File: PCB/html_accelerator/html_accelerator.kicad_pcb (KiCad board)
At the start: 4 copper layers, 456.8 x 111.2 mm, 45 parts, among them J1 PCIexpress_bracket, J2 Bus_PCI_Express_x8, J3 PCIexpress_bracket, U10 48-TSOPI_12X20_MAC, U7 48-TSOPI_12X20_MAC, U8 48-TSOPI_12X20_MAC, U9 48-TSOPI_12X20_MAC

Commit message: Sch Symbol updates and cleanup
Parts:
- U10, U8, U9: value 48-TSOPI_12X20_MAC -> MX30LF1G28AD-TI
- U2, U4, U5: value ~ -> AU6438BS
- U3: value ~ -> MX30LF1G28AD-TI; footprint Package_SO:SSOP-28_3.9x9.9mm_P0.635mm -> html_accel_footprints:MX30LF1G28AD-TI
- U7: value 48-TSOPI_12X20_MAC -> AU6438BS; footprint html_accel_footprints:MX30LF1G28AD-TI -> Package_SO:SSOP-28_3.9x9.9mm_P0.635mm
- moved U3 30.4 mm to (49.1, 42.2)
- moved U7 28.4 mm to (71.8, 59.3)
- moved U4 5.91 mm to (71.8, 76.6)
- moved U5 4.67 mm to (71.8, 98.1)
- moved U8 1.85 mm to (49.1, 60.8)
- moved U2 1.59 mm to (71.8, 41.9)
- moved U9 1.54 mm to (49.1, 79.3)
- moved U10 1.27 mm to (49.1, 97.9)
- moved U6 0.25 mm to (92.2, 95.8)
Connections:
- J3 pad 1: (no net) -> unconnected-(J3-PTH1-Pad1)
- J3 pad 2: (no net) -> unconnected-(J3-PTH2-Pad2)
- U10 pad 16: unconnected-(U10B-CLE-Pad16) -> Net-(U10B-CLE)
- U10 pad 17: unconnected-(U10B-ALE-Pad17) -> Net-(U10B-ALE)
- U10 pad 18: unconnected-(U10B-WE#-Pad18) -> Net-(U10B-WE#)
- U10 pad 19: unconnected-(U10B-WP#-Pad19) -> Net-(U10B-WP#)
- U10 pad 38: unconnected-(U10B-PT-Pad38) -> Net-(U10B-PT)
- U10 pad 8: unconnected-(U10B-RE#-Pad8) -> Net-(U10B-RE#)
- U2 pad 1: (no net) -> unconnected-(U2-SDCDN-Pad1)
- U2 pad 10: (no net) -> unconnected-(U2-XTAL_IN-Pad10)
- U2 pad 11: (no net) -> unconnected-(U2-XTAL_OUT-Pad11)
- U2 pad 12: (no net) -> unconnected-(U2-VSS-Pad12)
- U2 pad 13: (no net) -> unconnected-(U2-VDD_1.8_OUT-Pad13)
- U2 pad 14: (no net) -> unconnected-(U2-VDD_FLASH_3.3_OUT-Pad14)
- U2 pad 15: (no net) -> unconnected-(U2-AVDD_5.0_OUT-Pad15)
- U2 pad 16: (no net) -> unconnected-(U2-VDD__3.3_OUT-Pad16)
- U2 pad 17: (no net) -> unconnected-(U2-VSSHM-Pad17)
- U2 pad 18: (no net) -> unconnected-(U2-MSINS-Pad18)
- U2 pad 19: (no net) -> unconnected-(U2-DATA2-Pad19)
- U2 pad 2: (no net) -> unconnected-(U2-SDWP-Pad2)
- U2 pad 20: (no net) -> unconnected-(U2-DATA3-Pad20)
- U2 pad 21: (no net) -> unconnected-(U2-DATA4-Pad21)
- U2 pad 22: (no net) -> unconnected-(U2-SDCMD-Pad22)
- U2 pad 23: (no net) -> unconnected-(U2-DATA5-Pad23)
- U2 pad 24: (no net) -> unconnected-(U2-SD_CLK-Pad24)
- U2 pad 25: (no net) -> unconnected-(U2-DATA6-Pad25)
- U2 pad 26: (no net) -> unconnected-(U2-DATA7-Pad26)
- U2 pad 27: (no net) -> unconnected-(U2-DATA0-Pad27)
- U2 pad 28: (no net) -> unconnected-(U2-DATA1-Pad28)
- U2 pad 3: (no net) -> unconnected-(U2-LED_ACTIVITY-Pad3)
- U2 pad 4: (no net) -> unconnected-(U2-CHIP_RST_N-Pad4)
- U2 pad 5: (no net) -> unconnected-(U2-EXT_R-Pad5)
- U2 pad 6: (no net) -> unconnected-(U2-V3.3_PHY_IN-Pad6)
- U2 pad 7: (no net) -> unconnected-(U2-USB_DP-Pad7)
- U2 pad 8: (no net) -> unconnected-(U2-USB_DN-Pad8)
- U2 pad 9: (no net) -> unconnected-(U2-VSSAREG-Pad9)
- U3 pad 1: (no net) -> unconnected-(U3A-NC-Pad1)
- U3 pad 10: (no net) -> unconnected-(U3A-NC-Pad10)
- U3 pad 11: (no net) -> unconnected-(U3A-NC-Pad11)
- U3 pad 12: (no net) -> unconnected-(U3A-VCC-Pad12)
- U3 pad 13: (no net) -> unconnected-(U3A-VSS-Pad13)
- U3 pad 14: (no net) -> unconnected-(U3A-NC-Pad14)
- U3 pad 15: (no net) -> unconnected-(U3A-NC-Pad15)
- U3 pad 16: (no net) -> unconnected-(U3B-CLE-Pad16)
- U3 pad 17: (no net) -> unconnected-(U3B-ALE-Pad17)
- U3 pad 18: (no net) -> unconnected-(U3B-WE#-Pad18)
- U3 pad 19: (no net) -> unconnected-(U3B-WP#-Pad19)
- U3 pad 2: (no net) -> unconnected-(U3A-NC-Pad2)
- U3 pad 20: (no net) -> unconnected-(U3A-NC-Pad20)
- U3 pad 21: (no net) -> unconnected-(U3A-NC-Pad21)
- U3 pad 22: (no net) -> unconnected-(U3A-NC-Pad22)
- U3 pad 23: (no net) -> unconnected-(U3A-NC-Pad23)
- U3 pad 24: (no net) -> unconnected-(U3A-NC-Pad24)
- U3 pad 25: (no net) -> unconnected-(U3A-VSS-Pad25)
- U3 pad 26: (no net) -> unconnected-(U3A-NC-Pad26)
- U3 pad 27: (no net) -> unconnected-(U3A-NC-Pad27)
- U3 pad 28: (no net) -> unconnected-(U3A-NC-Pad28)
- U3 pad 3: (no net) -> unconnected-(U3A-NC-Pad3)
- U3 pad 4: (no net) -> unconnected-(U3A-NC-Pad4)
- U3 pad 5: (no net) -> unconnected-(U3A-NC-Pad5)
- U3 pad 6: (no net) -> unconnected-(U3A-NC-Pad6)
- U3 pad 7: (no net) -> Net-(U3B-R/B#)
- U3 pad 8: (no net) -> unconnected-(U3B-RE#-Pad8)
- U3 pad 9: (no net) -> unconnected-(U3B-CE#-Pad9)
- U4 pad 1: (no net) -> unconnected-(U4-SDCDN-Pad1)
- U4 pad 10: (no net) -> unconnected-(U4-XTAL_IN-Pad10)
- U4 pad 11: (no net) -> unconnected-(U4-XTAL_OUT-Pad11)
- U4 pad 12: (no net) -> unconnected-(U4-VSS-Pad12)
- U4 pad 13: (no net) -> unconnected-(U4-VDD_1.8_OUT-Pad13)
- U4 pad 14: (no net) -> unconnected-(U4-VDD_FLASH_3.3_OUT-Pad14)
- U4 pad 15: (no net) -> unconnected-(U4-AVDD_5.0_OUT-Pad15)
- U4 pad 16: (no net) -> unconnected-(U4-VDD__3.3_OUT-Pad16)
- U4 pad 17: (no net) -> unconnected-(U4-VSSHM-Pad17)
- U4 pad 18: (no net) -> unconnected-(U4-MSINS-Pad18)
- U4 pad 19: (no net) -> unconnected-(U4-DATA2-Pad19)
- U4 pad 2: (no net) -> unconnected-(U4-SDWP-Pad2)
- U4 pad 20: (no net) -> unconnected-(U4-DATA3-Pad20)
- U4 pad 21: (no net) -> unconnected-(U4-DATA4-Pad21)
- U4 pad 22: (no net) -> unconnected-(U4-SDCMD-Pad22)
- U4 pad 23: (no net) -> unconnected-(U4-DATA5-Pad23)
- U4 pad 24: (no net) -> unconnected-(U4-SD_CLK-Pad24)
- U4 pad 25: (no net) -> unconnected-(U4-DATA6-Pad25)
- U4 pad 26: (no net) -> unconnected-(U4-DATA7-Pad26)
- U4 pad 27: (no net) -> unconnected-(U4-DATA0-Pad27)
- U4 pad 28: (no net) -> unconnected-(U4-DATA1-Pad28)
- U4 pad 3: (no net) -> unconnected-(U4-LED_ACTIVITY-Pad3)
- U4 pad 4: (no net) -> unconnected-(U4-CHIP_RST_N-Pad4)
- U4 pad 5: (no net) -> unconnected-(U4-EXT_R-Pad5)
- U4 pad 6: (no net) -> unconnected-(U4-V3.3_PHY_IN-Pad6)
- U4 pad 7: (no net) -> unconnected-(U4-USB_DP-Pad7)
- U4 pad 8: (no net) -> unconnected-(U4-USB_DN-Pad8)
- U4 pad 9: (no net) -> unconnected-(U4-VSSAREG-Pad9)
- U5 pad 1: (no net) -> unconnected-(U5-SDCDN-Pad1)
- U5 pad 10: (no net) -> unconnected-(U5-XTAL_IN-Pad10)
- U5 pad 11: (no net) -> unconnected-(U5-XTAL_OUT-Pad11)
- U5 pad 12: (no net) -> unconnected-(U5-VSS-Pad12)
- U5 pad 13: (no net) -> unconnected-(U5-VDD_1.8_OUT-Pad13)
- U5 pad 14: (no net) -> unconnected-(U5-VDD_FLASH_3.3_OUT-Pad14)
- U5 pad 15: (no net) -> unconnected-(U5-AVDD_5.0_OUT-Pad15)
- U5 pad 16: (no net) -> unconnected-(U5-VDD__3.3_OUT-Pad16)
- U5 pad 17: (no net) -> unconnected-(U5-VSSHM-Pad17)
- U5 pad 18: (no net) -> unconnected-(U5-MSINS-Pad18)
- U5 pad 19: (no net) -> unconnected-(U5-DATA2-Pad19)
- U5 pad 2: (no net) -> unconnected-(U5-SDWP-Pad2)
- U5 pad 20: (no net) -> unconnected-(U5-DATA3-Pad20)
- U5 pad 21: (no net) -> unconnected-(U5-DATA4-Pad21)
- U5 pad 22: (no net) -> unconnected-(U5-SDCMD-Pad22)
- U5 pad 23: (no net) -> unconnected-(U5-DATA5-Pad23)
- U5 pad 24: (no net) -> unconnected-(U5-SD_CLK-Pad24)
- U5 pad 25: (no net) -> unconnected-(U5-DATA6-Pad25)
- U5 pad 26: (no net) -> unconnected-(U5-DATA7-Pad26)
- U5 pad 27: (no net) -> unconnected-(U5-DATA0-Pad27)
- U5 pad 28: (no net) -> unconnected-(U5-DATA1-Pad28)
- U5 pad 3: (no net) -> unconnected-(U5-LED_ACTIVITY-Pad3)
- U5 pad 4: (no net) -> unconnected-(U5-CHIP_RST_N-Pad4)
- U5 pad 5: (no net) -> unconnected-(U5-EXT_R-Pad5)
- U5 pad 6: (no net) -> unconnected-(U5-V3.3_PHY_IN-Pad6)
- U5 pad 7: (no net) -> unconnected-(U5-USB_DP-Pad7)
- U5 pad 8: (no net) -> unconnected-(U5-USB_DN-Pad8)
- U5 pad 9: (no net) -> unconnected-(U5-VSSAREG-Pad9)
- U8 pad 16: unconnected-(U8B-CLE-Pad16) -> Net-(U3B-I/O0)
- U8 pad 17: unconnected-(U8B-ALE-Pad17) -> Net-(U3B-R/B#)
- U8 pad 18: unconnected-(U8B-WE#-Pad18) -> Net-(U3B-I/O5)
- U8 pad 19: unconnected-(U8B-WP#-Pad19) -> Net-(U3B-I/O6)
- U8 pad 38: unconnected-(U8B-PT-Pad38) -> Net-(U3B-I/O1)
- U8 pad 8: unconnected-(U8B-RE#-Pad8) -> Net-(U3B-I/O3)
- U9 pad 29: unconnected-(U9B-I/O0-Pad29) -> Net-(U10B-CLE)
- U9 pad 30: unconnected-(U9B-I/O1-Pad30) -> Net-(U10B-PT)
- U9 pad 32: unconnected-(U9B-I/O3-Pad32) -> Net-(U10B-RE#)
- U9 pad 42: unconnected-(U9B-I/O5-Pad42) -> Net-(U10B-WE#)
- U9 pad 43: unconnected-(U9B-I/O6-Pad43) -> Net-(U10B-WP#)
- U9 pad 7: unconnected-(U9B-R/B#-Pad7) -> Net-(U10B-ALE)
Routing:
- net +12V: track 2.62 -> 0.00 mm, vias 2 -> 0
- net (no net): track 0.00 -> 2.62 mm, vias 0 -> 2

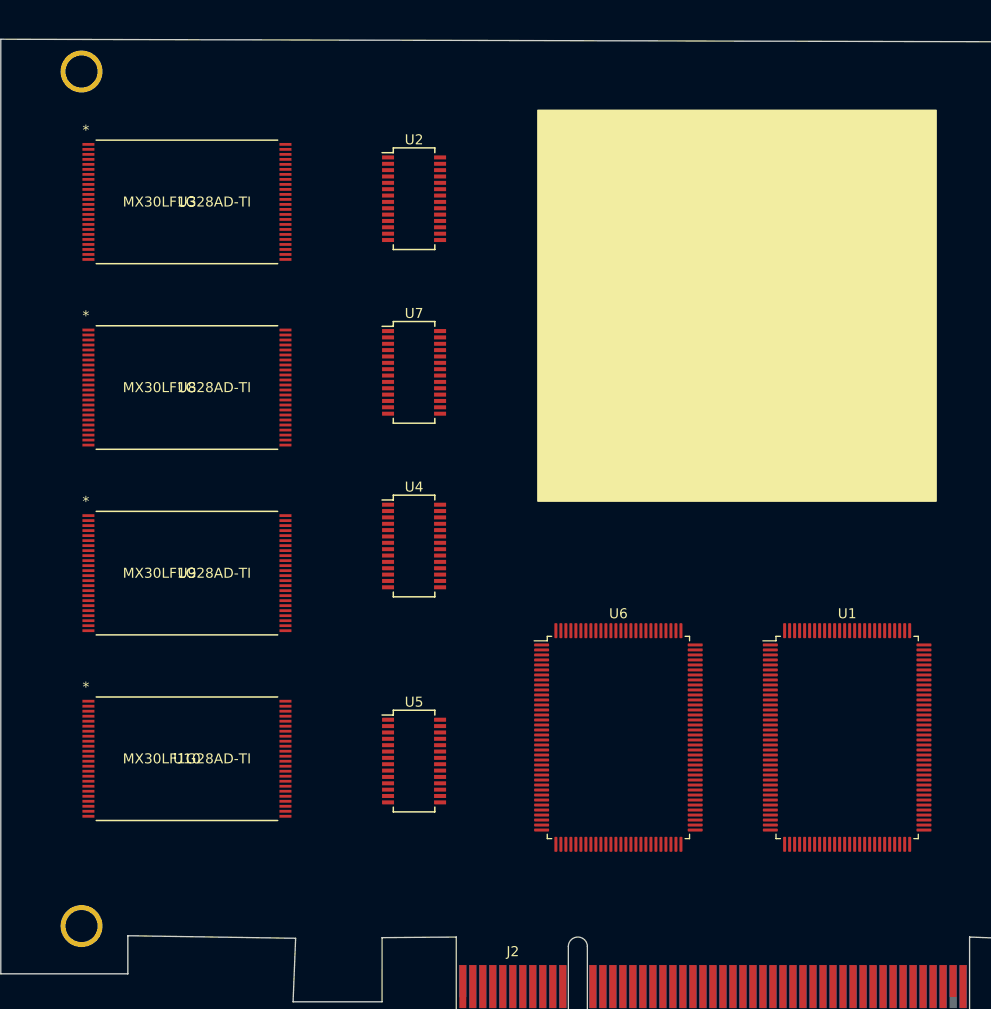
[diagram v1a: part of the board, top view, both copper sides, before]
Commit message: Update to MCS9990 for PCIE direct to USB
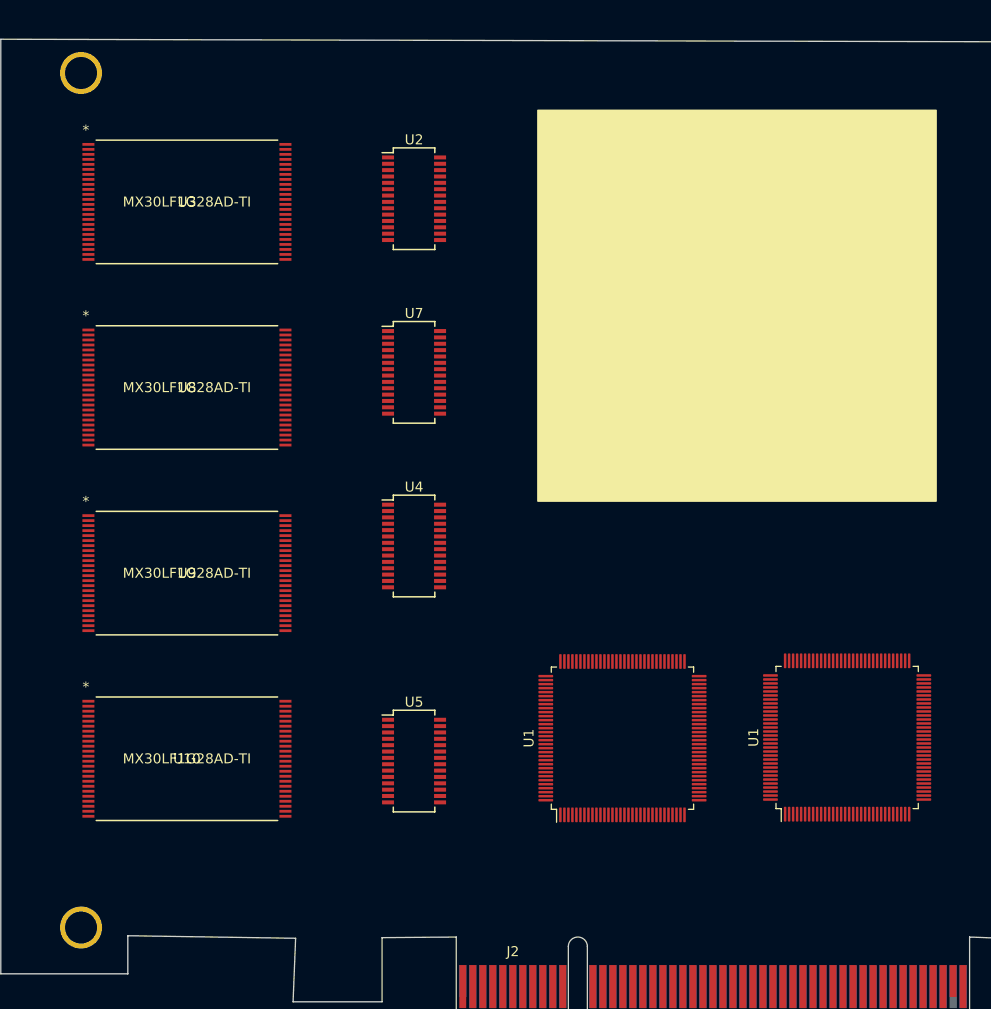
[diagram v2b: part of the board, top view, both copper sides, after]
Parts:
- removed J3: PCIexpress_bracket, html_accel_footprints:PCIexpress_bracket_full
- removed U6: ~, Package_QFP:LQFP-128_14x20mm_P0.5mm
- added U1: MCS9990, Package_QFP:LQFP-128_14x14mm_P0.4mm, F.Cu at (92.6, 95.8)
- J1: footprint PCIexpress:PCIexpress_bracket_full -> html_accel_footprints:PCIexpress_bracket_full
- U1: value ~ -> MCS9990; footprint Package_QFP:LQFP-128_14x20mm_P0.5mm -> Package_QFP:LQFP-128_14x14mm_P0.4mm
- moved J1 357.1 mm to (76.2, 124.1)
- turned U1 to 90 degrees
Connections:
- U1 pad 1: (no net) -> unconnected-(U1A-GND1-Pad1)
- U1 pad 10: (no net) -> unconnected-(U1C-PCIE_RXDP-Pad10)
- U1 pad 100: (no net) -> unconnected-(U1D-USB0_PWR_EN_N-Pad100)
- U1 pad 101: (no net) -> unconnected-(U1E-LN_STAT2-Pad101)
- U1 pad 102: (no net) -> unconnected-(U1D-USB1_OVCI_N-Pad102)
- U1 pad 103: (no net) -> unconnected-(U1D-USB1_PWR_EN_N-Pad103)
- U1 pad 104: (no net) -> unconnected-(U1E-LN_STAT0-Pad104)
- U1 pad 105: (no net) -> unconnected-(U1E-LN_STAT1-Pad105)
- U1 pad 106: (no net) -> unconnected-(U1A-+3.3VIO-Pad106)
- U1 pad 107: (no net) -> unconnected-(U1A-GND20-Pad107)
- U1 pad 108: (no net) -> unconnected-(U1A-GND21-Pad108)
- U1 pad 109: (no net) -> unconnected-(U1A-+1.2V-Pad109)
- U1 pad 11: (no net) -> unconnected-(U1A-GND3-Pad11)
- U1 pad 110: (no net) -> unconnected-(U1A-+3.3VA-Pad110)
- U1 pad 111: (no net) -> unconnected-(U1A-+3.3VA-Pad111)
- U1 pad 112: (no net) -> unconnected-(U1D-USB2_DM-Pad112)
- U1 pad 113: (no net) -> unconnected-(U1D-USB2_DP-Pad113)
- U1 pad 114: (no net) -> unconnected-(U1A-GND22-Pad114)
- U1 pad 115: (no net) -> unconnected-(U1A-GND23-Pad115)
- U1 pad 116: (no net) -> unconnected-(U1D-USB2_IBERF-Pad116)
- U1 pad 117: (no net) -> unconnected-(U1D-USB2_OTG_VBUS-Pad117)
- U1 pad 118: (no net) -> unconnected-(U1A-GND24-Pad118)
- U1 pad 119: (no net) -> unconnected-(U1A-+3.3VA-Pad119)
- U1 pad 12: (no net) -> unconnected-(U1A-+1.2VA-Pad12)
- U1 pad 120: (no net) -> unconnected-(U1A-GND25-Pad120)
- U1 pad 121: (no net) -> unconnected-(U1A-+1.2V-Pad121)
- U1 pad 122: (no net) -> unconnected-(U1D-USB2_OVCI_N-Pad122)
- U1 pad 123: (no net) -> unconnected-(U1D-USB2_PWR_EN_N-Pad123)
- U1 pad 124: (no net) -> unconnected-(U1D-USB2_OTG_ID-Pad124)
- U1 pad 125: (no net) -> unconnected-(U1D-USB3_OVCI_N-Pad125)
- U1 pad 126: (no net) -> unconnected-(U1D-USB3_PWR_EN_N-Pad126)
- U1 pad 127: (no net) -> unconnected-(U1A-+3.3VIO-Pad127)
- U1 pad 128: (no net) -> unconnected-(U1A-GND26-Pad128)
- U1 pad 13: (no net) -> unconnected-(U1C-PCIE_TXDP-Pad13)
- U1 pad 14: (no net) -> unconnected-(U1C-PCIE_TXDN-Pad14)
- U1 pad 15: (no net) -> unconnected-(U1A-+1.2VA-Pad15)
- U1 pad 16: (no net) -> unconnected-(U1A-+3.3VA_PLL-Pad16)
- U1 pad 17: (no net) -> unconnected-(U1A-GND4-Pad17)
- U1 pad 18: (no net) -> unconnected-(U1A-GND5-Pad18)
- U1 pad 19: (no net) -> unconnected-(U1A-+3.3VA_AUX-Pad19)
- U1 pad 2: (no net) -> unconnected-(U1A-+3.3VIN_REG-Pad2)
- U1 pad 20: (no net) -> unconnected-(U1A-+1.2V-Pad20)
- U1 pad 21: (no net) -> unconnected-(U1A-GND6-Pad21)
- U1 pad 22: (no net) -> unconnected-(U1C-PCIE_CLKREQ_N-Pad22)
- U1 pad 23: (no net) -> unconnected-(U1C-PCIE_WAKE_N-Pad23)
- U1 pad 24: (no net) -> unconnected-(U1E-MODE_SEL0-Pad24)
- U1 pad 25: (no net) -> unconnected-(U1A-+3.3VIO-Pad25)
- U1 pad 26: (no net) -> unconnected-(U1A-GND7-Pad26)
- U1 pad 27: (no net) -> unconnected-(U1E-OTG_EN_N-Pad27)
- U1 pad 28: (no net) -> unconnected-(U1C-PCIE_PERST_N-Pad28)
- U1 pad 29: (no net) -> unconnected-(U1E-EE_SCL-Pad29)
- U1 pad 3: (no net) -> unconnected-(U1A-+1.2VOUT_REG-Pad3)
- U1 pad 30: (no net) -> unconnected-(U1E-EE_SDA-Pad30)
- U1 pad 31: (no net) -> unconnected-(U1E-SCAN_EN-Pad31)
- U1 pad 32: (no net) -> unconnected-(U1E-TEST_EN-Pad32)
- U1 pad 33: (no net) -> unconnected-(U1A-+1.2V-Pad33)
- U1 pad 34: (no net) -> unconnected-(U1A-GND8-Pad34)
- U1 pad 35: (no net) -> unconnected-(U1B-GPIO0/D0-Pad35)
- U1 pad 36: (no net) -> unconnected-(U1B-GPIO1/D1-Pad36)
- U1 pad 37: (no net) -> unconnected-(U1B-GPIO2/D2-Pad37)
- U1 pad 38: (no net) -> unconnected-(U1B-GPIO3/D3-Pad38)
- U1 pad 39: (no net) -> unconnected-(U1B-GPIO4/D4-Pad39)
- U1 pad 4: (no net) -> unconnected-(U1C-PCIE_REFCLKN-Pad4)
- U1 pad 40: (no net) -> unconnected-(U1B-GPIO5/D5-Pad40)
- U1 pad 41: (no net) -> unconnected-(U1B-GPIO6/D6-Pad41)
- U1 pad 42: (no net) -> unconnected-(U1B-GPIO7/D7-Pad42)
- U1 pad 43: (no net) -> unconnected-(U1B-GPIO8/INTA-Pad43)
- U1 pad 44: (no net) -> unconnected-(U1B-GPIO9/INTB-Pad44)
- U1 pad 45: (no net) -> unconnected-(U1B-GPIO10/INTC-Pad45)
- U1 pad 46: (no net) -> unconnected-(U1B-GPIO11/INTD-Pad46)
- U1 pad 47: (no net) -> unconnected-(U1E-MODE_SEL1-Pad47)
- U1 pad 48: (no net) -> unconnected-(U1A-+3.3VIO-Pad48)
- U1 pad 49: (no net) -> unconnected-(U1E-MODE_SEL2-Pad49)
- U1 pad 5: (no net) -> unconnected-(U1C-PCIE_REFCLKP-Pad5)
- U1 pad 50: (no net) -> unconnected-(U1A-GND9-Pad50)
- U1 pad 51: (no net) -> unconnected-(U1A-+3.3VA-Pad51)
- U1 pad 52: (no net) -> unconnected-(U1A-+3.3VA-Pad52)
- U1 pad 53: (no net) -> unconnected-(U1D-USB3_DM-Pad53)
- U1 pad 54: (no net) -> unconnected-(U1D-USB3_DP-Pad54)
- U1 pad 55: (no net) -> unconnected-(U1A-GND10-Pad55)
- U1 pad 56: (no net) -> unconnected-(U1A-GND11-Pad56)
- U1 pad 57: (no net) -> unconnected-(U1D-USB3_IBREF-Pad57)
- U1 pad 58: (no net) -> unconnected-(U1A-+1.2V-Pad58)
- U1 pad 59: (no net) -> unconnected-(U1A-GND12-Pad59)
- U1 pad 6: (no net) -> unconnected-(U1A-+1.2VA_AUX-Pad6)
- U1 pad 60: (no net) -> unconnected-(U1E-JTAG_TCK-Pad60)
- U1 pad 61: (no net) -> unconnected-(U1E-JTAG_TDI-Pad61)
- U1 pad 62: (no net) -> unconnected-(U1E-JTAG_TDO-Pad62)
- U1 pad 63: (no net) -> unconnected-(U1E-JTAG_TMS-Pad63)
- U1 pad 64: (no net) -> unconnected-(U1E-JTAG_TRST_N-Pad64)
- U1 pad 65: (no net) -> unconnected-(U1B-GPIO12/CSA_N-Pad65)
- U1 pad 66: (no net) -> unconnected-(U1B-GPIO13/CSB_N-Pad66)
- U1 pad 67: (no net) -> unconnected-(U1B-GPIO14/CSC_N-Pad67)
- U1 pad 68: (no net) -> unconnected-(U1B-GPIO15/CSD_N-Pad68)
- U1 pad 69: (no net) -> unconnected-(U1A-GND13-Pad69)
- U1 pad 7: (no net) -> unconnected-(U1C-REXT-Pad7)
- U1 pad 70: (no net) -> unconnected-(U1A-+3.3VIO-Pad70)
- U1 pad 71: (no net) -> unconnected-(U1B-GPIO16/RESET-Pad71)
- U1 pad 72: (no net) -> unconnected-(U1B-GPIO17/IOW_N-Pad72)
- U1 pad 73: (no net) -> unconnected-(U1B-GPIO18/IOR_N-Pad73)
- U1 pad 74: (no net) -> unconnected-(U1B-GPIO23/IOCHRDY2-Pad74)
- U1 pad 75: (no net) -> unconnected-(U1B-GPIO19/A0-Pad75)
- U1 pad 76: (no net) -> unconnected-(U1B-GPIO20/A1-Pad76)
- U1 pad 77: (no net) -> unconnected-(U1B-GPIO21/A2-Pad77)
- U1 pad 78: (no net) -> unconnected-(U1B-GPIO22/IOCHRDY1-Pad78)
- U1 pad 79: (no net) -> unconnected-(U1A-GND14-Pad79)
- U1 pad 8: (no net) -> unconnected-(U1A-GND2-Pad8)
- U1 pad 80: (no net) -> unconnected-(U1A-+1.2V-Pad80)
- U1 pad 81: (no net) -> unconnected-(U1D-USB0_XSCI-Pad81)
- U1 pad 82: (no net) -> unconnected-(U1D-USB0_XSCO-Pad82)
- U1 pad 83: (no net) -> unconnected-(U1A-+3.3VA-Pad83)
- U1 pad 84: (no net) -> unconnected-(U1A-+3.3VA-Pad84)
- U1 pad 85: (no net) -> unconnected-(U1D-USB0_DM-Pad85)
- U1 pad 86: (no net) -> unconnected-(U1D-USB0_DP-Pad86)
- U1 pad 87: (no net) -> unconnected-(U1A-GND15-Pad87)
- U1 pad 88: (no net) -> unconnected-(U1A-GND16-Pad88)
- U1 pad 89: (no net) -> unconnected-(U1D-USB0_IBREF-Pad89)
- U1 pad 9: (no net) -> unconnected-(U1C-PCIE_RXDN-Pad9)
- U1 pad 90: (no net) -> unconnected-(U1A-+3.3VA-Pad90)
- U1 pad 91: (no net) -> unconnected-(U1A-+3.3VA-Pad91)
- U1 pad 92: (no net) -> unconnected-(U1D-USB1_DM-Pad92)
- U1 pad 93: (no net) -> unconnected-(U1D-USB1_DP-Pad93)
- U1 pad 94: (no net) -> unconnected-(U1A-GND17-Pad94)
- U1 pad 95: (no net) -> unconnected-(U1A-GND18-Pad95)
- U1 pad 96: (no net) -> unconnected-(U1D-USB1_IBREF-Pad96)
- U1 pad 97: (no net) -> unconnected-(U1A-GND19-Pad97)
- U1 pad 98: (no net) -> unconnected-(U1A-+1.2V-Pad98)
- U1 pad 99: (no net) -> unconnected-(U1D-USB0_OVCI_N-Pad99)
- U10 pad 16: Net-(U10B-CLE) -> unconnected-(U10B-#CMD_LATCH_EN-Pad16)
- U10 pad 17: Net-(U10B-ALE) -> unconnected-(U10B-ADDR_LATCH-Pad17)
- U10 pad 18: Net-(U10B-WE#) -> unconnected-(U10B-#WRITE_EN-Pad18)
- U10 pad 19: Net-(U10B-WP#) -> unconnected-(U10B-#WRITE_PROT-Pad19)
- U10 pad 38: Net-(U10B-PT) -> unconnected-(U10B-PROTECT-Pad38)
- U10 pad 8: Net-(U10B-RE#) -> unconnected-(U10B-#READ_EN-Pad8)
- U3 pad 29: Net-(U3B-I/O0) -> unconnected-(U3B-I/O0-Pad29)
- U3 pad 30: Net-(U3B-I/O1) -> unconnected-(U3B-I/O1-Pad30)
- U3 pad 32: Net-(U3B-I/O3) -> unconnected-(U3B-I/O3-Pad32)
- U3 pad 42: Net-(U3B-I/O5) -> unconnected-(U3B-I/O5-Pad42)
- U3 pad 43: Net-(U3B-I/O6) -> unconnected-(U3B-I/O6-Pad43)
- U3 pad 7: Net-(U3B-R/B#) -> unconnected-(U3B-STATUS-Pad7)
- U8 pad 16: Net-(U3B-I/O0) -> unconnected-(U8B-#CMD_LATCH_EN-Pad16)
- U8 pad 17: Net-(U3B-R/B#) -> unconnected-(U8B-ADDR_LATCH-Pad17)
- U8 pad 18: Net-(U3B-I/O5) -> unconnected-(U8B-#WRITE_EN-Pad18)
- U8 pad 19: Net-(U3B-I/O6) -> unconnected-(U8B-#WRITE_PROT-Pad19)
- U8 pad 38: Net-(U3B-I/O1) -> unconnected-(U8B-PROTECT-Pad38)
- U8 pad 8: Net-(U3B-I/O3) -> unconnected-(U8B-#READ_EN-Pad8)
- U9 pad 29: Net-(U10B-CLE) -> unconnected-(U9B-I/O0-Pad29)
- U9 pad 30: Net-(U10B-PT) -> unconnected-(U9B-I/O1-Pad30)
- U9 pad 32: Net-(U10B-RE#) -> unconnected-(U9B-I/O3-Pad32)
- U9 pad 42: Net-(U10B-WE#) -> unconnected-(U9B-I/O5-Pad42)
- U9 pad 43: Net-(U10B-WP#) -> unconnected-(U9B-I/O6-Pad43)
- U9 pad 7: Net-(U10B-ALE) -> unconnected-(U9B-STATUS-Pad7)
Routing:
- net Net-(J2-+12V-PadA2): track 0.00 -> 2.62 mm, vias 0 -> 2
- net (no net): track 2.62 -> 0.00 mm, vias 2 -> 0

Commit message: 3d part models, PCB netlist imported
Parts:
- removed the U1 at (92.6, 95.8)
- removed the U1 at (115.1, 95.8)
- added C17: 0.1uF, Capacitor_SMD:C_0805_2012Metric_Pad1.18x1.45mm_HandSolder, F.Cu at (56.1, 90.6)
- added C18: 0.1uF, Capacitor_SMD:C_0805_2012Metric_Pad1.18x1.45mm_HandSolder, F.Cu at (56.1, 93.6)
- added C19: 0.1uF, Capacitor_SMD:C_0805_2012Metric_Pad1.18x1.45mm_HandSolder, F.Cu at (60.9, 72.5)
- added C20: 0.1uF, Capacitor_SMD:C_0805_2012Metric_Pad1.18x1.45mm_HandSolder, F.Cu at (60.9, 75.5)
- added C21: 10uF, Capacitor_SMD:C_0805_2012Metric_Pad1.18x1.45mm_HandSolder, F.Cu at (60.9, 78.5)
- added C22: 0.1uF, Capacitor_SMD:C_0805_2012Metric_Pad1.18x1.45mm_HandSolder, F.Cu at (60.9, 81.5)
- added C23: 0.1uF, Capacitor_SMD:C_0805_2012Metric_Pad1.18x1.45mm_HandSolder, F.Cu at (60.9, 84.5)
- added C24: 0.1uF, Capacitor_SMD:C_0805_2012Metric_Pad1.18x1.45mm_HandSolder, F.Cu at (60.9, 87.5)
- added C25: 0.1uF, Capacitor_SMD:C_0805_2012Metric_Pad1.18x1.45mm_HandSolder, F.Cu at (60.9, 90.6)
- added C26: 10uF, Capacitor_SMD:C_0805_2012Metric_Pad1.18x1.45mm_HandSolder, F.Cu at (60.9, 93.6)
- added C27: 0.1uF, Capacitor_SMD:C_0805_2012Metric_Pad1.18x1.45mm_HandSolder, F.Cu at (65.7, 72.5)
- added C28: 0.1uF, Capacitor_SMD:C_0805_2012Metric_Pad1.18x1.45mm_HandSolder, F.Cu at (65.7, 75.5)
- added C29: 0.1uF, Capacitor_SMD:C_0805_2012Metric_Pad1.18x1.45mm_HandSolder, F.Cu at (65.7, 78.5)
- added C30: 0.1uF, Capacitor_SMD:C_0805_2012Metric_Pad1.18x1.45mm_HandSolder, F.Cu at (65.7, 81.5)
- added C31: 0.1uF, Capacitor_SMD:C_0805_2012Metric_Pad1.18x1.45mm_HandSolder, F.Cu at (65.7, 84.5)
- added C32: 0.1uF, Capacitor_SMD:C_0805_2012Metric_Pad1.18x1.45mm_HandSolder, F.Cu at (66.9, 44.0)
- added C33: 470uF, Capacitor_SMD:C_0805_2012Metric_Pad1.18x1.45mm_HandSolder, F.Cu at (66.9, 47.0)
- added C34: 470uF, Capacitor_SMD:C_0805_2012Metric_Pad1.18x1.45mm_HandSolder, F.Cu at (66.9, 50.1)
- added C35: 0.1uF, Capacitor_SMD:C_0805_2012Metric_Pad1.18x1.45mm_HandSolder, F.Cu at (36.5, 58.1)
- added C36: 22pF, Capacitor_SMD:C_0805_2012Metric_Pad1.18x1.45mm_HandSolder, F.Cu at (36.5, 61.1)
- added C37: 22pF, Capacitor_SMD:C_0805_2012Metric_Pad1.18x1.45mm_HandSolder, F.Cu at (36.5, 64.1)
- added C38: 4.7uF, Capacitor_SMD:C_0805_2012Metric_Pad1.18x1.45mm_HandSolder, F.Cu at (31.8, 17.8)
- added C39: 4.7uF, Capacitor_SMD:C_0805_2012Metric_Pad1.18x1.45mm_HandSolder, F.Cu at (31.8, 20.8)
- added C40: 22pF, Capacitor_SMD:C_0805_2012Metric_Pad1.18x1.45mm_HandSolder, F.Cu at (31.8, 23.9)
- added C41: 22pF, Capacitor_SMD:C_0805_2012Metric_Pad1.18x1.45mm_HandSolder, F.Cu at (31.8, 26.9)
- added C42: 2.2uF, Capacitor_SMD:C_0805_2012Metric_Pad1.18x1.45mm_HandSolder, F.Cu at (31.8, 29.9)
- added C43: 2.2uF, Capacitor_SMD:C_0805_2012Metric_Pad1.18x1.45mm_HandSolder, F.Cu at (31.8, 32.9)
- added C44: 0.1uF, Capacitor_SMD:C_0805_2012Metric_Pad1.18x1.45mm_HandSolder, F.Cu at (31.8, 35.9)
- added C45: 4.7uF, Capacitor_SMD:C_0805_2012Metric_Pad1.18x1.45mm_HandSolder, F.Cu at (77.3, 72.5)
- added C46: 4.7uF, Capacitor_SMD:C_0805_2012Metric_Pad1.18x1.45mm_HandSolder, F.Cu at (77.3, 75.5)
- added C47: 22pF, Capacitor_SMD:C_0805_2012Metric_Pad1.18x1.45mm_HandSolder, F.Cu at (77.3, 78.5)
- added C48: 22pF, Capacitor_SMD:C_0805_2012Metric_Pad1.18x1.45mm_HandSolder, F.Cu at (77.3, 81.5)
- added C49: 2.2uF, Capacitor_SMD:C_0805_2012Metric_Pad1.18x1.45mm_HandSolder, F.Cu at (77.3, 84.5)
- added C50: 2.2uF, Capacitor_SMD:C_0805_2012Metric_Pad1.18x1.45mm_HandSolder, F.Cu at (77.3, 87.5)
- added C51: 0.1uF, Capacitor_SMD:C_0805_2012Metric_Pad1.18x1.45mm_HandSolder, F.Cu at (77.3, 90.6)
- added C52: 4.7uF, Capacitor_SMD:C_0805_2012Metric_Pad1.18x1.45mm_HandSolder, F.Cu at (80.7, 17.8)
- added C53: 4.7uF, Capacitor_SMD:C_0805_2012Metric_Pad1.18x1.45mm_HandSolder, F.Cu at (80.7, 20.8)
- added C54: 22pF, Capacitor_SMD:C_0805_2012Metric_Pad1.18x1.45mm_HandSolder, F.Cu at (80.7, 23.9)
- added C55: 22pF, Capacitor_SMD:C_0805_2012Metric_Pad1.18x1.45mm_HandSolder, F.Cu at (80.7, 26.9)
- added C56: 2.2uF, Capacitor_SMD:C_0805_2012Metric_Pad1.18x1.45mm_HandSolder, F.Cu at (80.7, 29.9)
- added C57: 2.2uF, Capacitor_SMD:C_0805_2012Metric_Pad1.18x1.45mm_HandSolder, F.Cu at (80.7, 32.9)
- added C58: 0.1uF, Capacitor_SMD:C_0805_2012Metric_Pad1.18x1.45mm_HandSolder, F.Cu at (80.7, 35.9)
- added C59: 4.7uF, Capacitor_SMD:C_0805_2012Metric_Pad1.18x1.45mm_HandSolder, F.Cu at (51.3, 17.8)
- added C60: 4.7uF, Capacitor_SMD:C_0805_2012Metric_Pad1.18x1.45mm_HandSolder, F.Cu at (51.3, 20.8)
- added C61: 22pF, Capacitor_SMD:C_0805_2012Metric_Pad1.18x1.45mm_HandSolder, F.Cu at (51.3, 23.9)
- added C62: 22pF, Capacitor_SMD:C_0805_2012Metric_Pad1.18x1.45mm_HandSolder, F.Cu at (51.3, 26.9)
- added C63: 2.2uF, Capacitor_SMD:C_0805_2012Metric_Pad1.18x1.45mm_HandSolder, F.Cu at (51.3, 29.9)
- added C64: 2.2uF, Capacitor_SMD:C_0805_2012Metric_Pad1.18x1.45mm_HandSolder, F.Cu at (51.3, 32.9)
- added C65: 0.1uF, Capacitor_SMD:C_0805_2012Metric_Pad1.18x1.45mm_HandSolder, F.Cu at (51.3, 35.9)
- added C66: 0.1uF, Capacitor_SMD:C_0805_2012Metric_Pad1.18x1.45mm_HandSolder, F.Cu at (17.5, 87.8)
- added C67: 470uF, Capacitor_SMD:C_0805_2012Metric_Pad1.18x1.45mm_HandSolder, F.Cu at (17.5, 90.8)
- added D1: SBR2U30P1, html_accel_footprints:DIODE_SBR3M30P1_1P78X2P8_DIO-M, F.Cu at (66.5, 65.8)
- added D2: RED, LED_SMD:LED_0805_2012Metric_Pad1.15x1.40mm_HandSolder, F.Cu at (17.5, 93.9)
- added FB1: BLM21PG121SN1D, Resistor_SMD:R_0805_2012Metric_Pad1.20x1.40mm_HandSolder, F.Cu at (70.5, 72.5)
- added FB2: BLM21PG121SN1D, Resistor_SMD:R_0805_2012Metric_Pad1.20x1.40mm_HandSolder, F.Cu at (70.5, 75.4)
- added FB3: BLM21PG121SN1D, Resistor_SMD:R_0805_2012Metric_Pad1.20x1.40mm_HandSolder, F.Cu at (70.5, 78.4)
- added FB4: BLM21PG121SN1D, Resistor_SMD:R_0805_2012Metric_Pad1.20x1.40mm_HandSolder, F.Cu at (70.5, 81.3)
- added L1: SRR1208-330YL, html_accel_footprints:IND_BOURNS_SRR1208, F.Cu at (56.7, 49.9)
- added R17: 12k, Resistor_SMD:R_0805_2012Metric_Pad1.20x1.40mm_HandSolder, F.Cu at (56.0, 67.5)
- added R18: 3k, Resistor_SMD:R_0805_2012Metric_Pad1.20x1.40mm_HandSolder, F.Cu at (60.8, 58.7)
- added R19: 6.8k, Resistor_SMD:R_0805_2012Metric_Pad1.20x1.40mm_HandSolder, F.Cu at (60.8, 61.6)
- added R20: 1k, Resistor_SMD:R_0805_2012Metric_Pad1.20x1.40mm_HandSolder, F.Cu at (60.8, 64.6)
- added R21: 1.3k, Resistor_SMD:R_0805_2012Metric_Pad1.20x1.40mm_HandSolder, F.Cu at (60.8, 67.5)
- added R22: 4.7k, Resistor_SMD:R_0805_2012Metric_Pad1.20x1.40mm_HandSolder, F.Cu at (17.5, 58.1)
- added R23: 4.7k, Resistor_SMD:R_0805_2012Metric_Pad1.20x1.40mm_HandSolder, F.Cu at (17.5, 61.0)
- added R24: 4.7k, Resistor_SMD:R_0805_2012Metric_Pad1.20x1.40mm_HandSolder, F.Cu at (17.5, 64.0)
- added R25: 1k, Resistor_SMD:R_0805_2012Metric_Pad1.20x1.40mm_HandSolder, F.Cu at (17.5, 66.9)
- added R26: 1k, Resistor_SMD:R_0805_2012Metric_Pad1.20x1.40mm_HandSolder, F.Cu at (17.5, 69.9)
- added R27: 4.7k, Resistor_SMD:R_0805_2012Metric_Pad1.20x1.40mm_HandSolder, F.Cu at (22.2, 58.1)
- added R28: 1k, Resistor_SMD:R_0805_2012Metric_Pad1.20x1.40mm_HandSolder, F.Cu at (22.2, 61.0)
- added R29: 1k, Resistor_SMD:R_0805_2012Metric_Pad1.20x1.40mm_HandSolder, F.Cu at (22.2, 64.0)
- added R30: 1k, Resistor_SMD:R_0805_2012Metric_Pad1.20x1.40mm_HandSolder, F.Cu at (22.2, 66.9)
- added R31: 1k, Resistor_SMD:R_0805_2012Metric_Pad1.20x1.40mm_HandSolder, F.Cu at (22.2, 69.9)
- added R32: 1k, Resistor_SMD:R_0805_2012Metric_Pad1.20x1.40mm_HandSolder, F.Cu at (27.0, 58.1)
- added R33: 1k, Resistor_SMD:R_0805_2012Metric_Pad1.20x1.40mm_HandSolder, F.Cu at (27.0, 61.0)
- added R34: 1k, Resistor_SMD:R_0805_2012Metric_Pad1.20x1.40mm_HandSolder, F.Cu at (27.0, 64.0)
- added R35: 1k, Resistor_SMD:R_0805_2012Metric_Pad1.20x1.40mm_HandSolder, F.Cu at (27.0, 66.9)
- added R36: 1k, Resistor_SMD:R_0805_2012Metric_Pad1.20x1.40mm_HandSolder, F.Cu at (27.0, 69.9)
- added R37: 1k, Resistor_SMD:R_0805_2012Metric_Pad1.20x1.40mm_HandSolder, F.Cu at (31.7, 58.1)
- added R38: 1k, Resistor_SMD:R_0805_2012Metric_Pad1.20x1.40mm_HandSolder, F.Cu at (31.7, 61.0)
- added R39: 1k, Resistor_SMD:R_0805_2012Metric_Pad1.20x1.40mm_HandSolder, F.Cu at (31.7, 64.0)
- added R40: 1k, Resistor_SMD:R_0805_2012Metric_Pad1.20x1.40mm_HandSolder, F.Cu at (31.7, 66.9)
- added R41: 1k, Resistor_SMD:R_0805_2012Metric_Pad1.20x1.40mm_HandSolder, F.Cu at (31.7, 69.9)
- added R42: 10k, Resistor_SMD:R_0805_2012Metric_Pad1.20x1.40mm_HandSolder, F.Cu at (36.6, 17.8)
- added R43: 1k, Resistor_SMD:R_0805_2012Metric_Pad1.20x1.40mm_HandSolder, F.Cu at (36.6, 20.8)
- added R44: 27, Resistor_SMD:R_0805_2012Metric_Pad1.20x1.40mm_HandSolder, F.Cu at (36.6, 23.7)
- added R45: 680, Resistor_SMD:R_0805_2012Metric_Pad1.20x1.40mm_HandSolder, F.Cu at (36.6, 26.7)
- added R46: 10k, Resistor_SMD:R_0805_2012Metric_Pad1.20x1.40mm_HandSolder, F.Cu at (82.1, 78.7)
- added R47: 1k, Resistor_SMD:R_0805_2012Metric_Pad1.20x1.40mm_HandSolder, F.Cu at (82.1, 81.7)
- added R48: 27, Resistor_SMD:R_0805_2012Metric_Pad1.20x1.40mm_HandSolder, F.Cu at (82.1, 84.6)
- added R49: 680, Resistor_SMD:R_0805_2012Metric_Pad1.20x1.40mm_HandSolder, F.Cu at (82.1, 87.6)
- added R50: 10k, Resistor_SMD:R_0805_2012Metric_Pad1.20x1.40mm_HandSolder, F.Cu at (85.5, 24.1)
- added R51: 1k, Resistor_SMD:R_0805_2012Metric_Pad1.20x1.40mm_HandSolder, F.Cu at (85.5, 27.0)
- added R52: 27, Resistor_SMD:R_0805_2012Metric_Pad1.20x1.40mm_HandSolder, F.Cu at (85.5, 30.0)
- added R53: 680, Resistor_SMD:R_0805_2012Metric_Pad1.20x1.40mm_HandSolder, F.Cu at (85.5, 32.9)
- added R54: 10k, Resistor_SMD:R_0805_2012Metric_Pad1.20x1.40mm_HandSolder, F.Cu at (70.3, 17.8)
- added R55: 1k, Resistor_SMD:R_0805_2012Metric_Pad1.20x1.40mm_HandSolder, F.Cu at (70.3, 20.8)
- added R56: 27, Resistor_SMD:R_0805_2012Metric_Pad1.20x1.40mm_HandSolder, F.Cu at (70.3, 23.7)
- added R57: 680, Resistor_SMD:R_0805_2012Metric_Pad1.20x1.40mm_HandSolder, F.Cu at (70.3, 26.7)
- added R66: 3k, Resistor_SMD:R_0805_2012Metric_Pad1.20x1.40mm_HandSolder, F.Cu at (22.3, 87.8)
- added RN1: 1k, Resistor_SMD:R_Array_Convex_4x1206, F.Cu at (17.9, 74.7)
- added RN2: 1k, Resistor_SMD:R_Array_Convex_4x1206, F.Cu at (23.3, 74.7)
- added RN3: 1k, Resistor_SMD:R_Array_Convex_4x1206, F.Cu at (28.8, 74.7)
- added RN4: 1k, Resistor_SMD:R_Array_Convex_4x1206, F.Cu at (34.2, 74.7)
- added RN5: 1k, Resistor_SMD:R_Array_Convex_4x1206, F.Cu at (39.7, 74.7)
- added U1: MCS9990, Package_QFP:LQFP-128_14x14mm_P0.4mm, F.Cu at (87.7, 51.7)
- added U11: EMMC_4G, html_accel_footprints:EMMC04G-M627-X03U_KNT, F.Cu at (60.8, 22.7)
- added U6: EMMC_4G, html_accel_footprints:EMMC04G-M627-X03U_KNT, F.Cu at (22.2, 35.5)
- added Y1: 12MHz, Crystal:Crystal_SMD_HC49-SD, F.Cu at (22.4, 81.2)
- added Y2: 12MHz, Crystal:Crystal_SMD_HC49-SD, F.Cu at (36.7, 40.5)
- added Y3: 12MHz, Crystal:Crystal_SMD_HC49-SD, F.Cu at (87.0, 74.1)
- added Y4: 12MHz, Crystal:Crystal_SMD_HC49-SD, F.Cu at (90.4, 19.5)
- added Y5: 12MHz, Crystal:Crystal_SMD_HC49-SD, F.Cu at (69.0, 32.2)
- C1, C10, C11, C12, C13, C15, C16, C2, C4, C6, C8, C9: value 100n -> 0.1uF; footprint Capacitor_SMD:C_0603_1608Metric -> Capacitor_SMD:C_0805_2012Metric_Pad1.18x1.45mm_HandSolder; moved to F.Cu
- C14, C3, C7: value 100n -> 10uF; footprint Capacitor_SMD:C_0603_1608Metric -> Capacitor_SMD:C_0805_2012Metric_Pad1.18x1.45mm_HandSolder; moved to F.Cu
- C5: value 100n -> 3.3uF; footprint Capacitor_SMD:C_0603_1608Metric -> Capacitor_SMD:C_0805_2012Metric_Pad1.18x1.45mm_HandSolder; moved to F.Cu
- J1: value PCIexpress_bracket -> Bus_PCI_Express_x8; footprint html_accel_footprints:PCIexpress_bracket_full -> Connector_PCBEdge:BUS_PCIexpress_x8
- J2: value Bus_PCI_Express_x8 -> PCIexpress_bracket; footprint Connector_PCBEdge:BUS_PCIexpress_x8 -> html_accel_footprints:PCIexpress_bracket_full
- R1, R2, R3: value 49.9 -> 4.7k; footprint Resistor_SMD:R_0603_1608Metric -> Resistor_SMD:R_0805_2012Metric_Pad1.20x1.40mm_HandSolder
- R10, R11, R12, R13: value 49.9 -> 10k; footprint Resistor_SMD:R_0603_1608Metric -> Resistor_SMD:R_0805_2012Metric_Pad1.20x1.40mm_HandSolder
- R14, R15, R16: value 49.9 -> 12k; footprint Resistor_SMD:R_0603_1608Metric -> Resistor_SMD:R_0805_2012Metric_Pad1.20x1.40mm_HandSolder
- R4: value 49.9 -> 33; footprint Resistor_SMD:R_0603_1608Metric -> Resistor_SMD:R_0805_2012Metric_Pad1.20x1.40mm_HandSolder
- R5, R6, R9: value 49.9 -> 0; footprint Resistor_SMD:R_0603_1608Metric -> Resistor_SMD:R_0805_2012Metric_Pad1.20x1.40mm_HandSolder
- R7: value 49.9 -> 6.2k; footprint Resistor_SMD:R_0603_1608Metric -> Resistor_SMD:R_0805_2012Metric_Pad1.20x1.40mm_HandSolder
- R8: value 49.9 -> 1k; footprint Resistor_SMD:R_0603_1608Metric -> Resistor_SMD:R_0805_2012Metric_Pad1.20x1.40mm_HandSolder
- U10, U8, U9: value MX30LF1G28AD-TI -> AU6438BS; footprint html_accel_footprints:MX30LF1G28AD-TI -> Package_SO:SSOP-28_3.9x9.9mm_P0.635mm
- U2: value AU6438BS -> AP1513; footprint Package_SO:SSOP-28_3.9x9.9mm_P0.635mm -> html_accel_footprints:SOP-8L_DIO
- U3: value MX30LF1G28AD-TI -> CAT24C256YI-GT3; footprint html_accel_footprints:MX30LF1G28AD-TI -> Package_SO:TSSOP-8_4.4x3mm_P0.65mm
- U5, U7: value AU6438BS -> EMMC_4G; footprint Package_SO:SSOP-28_3.9x9.9mm_P0.635mm -> html_accel_footprints:EMMC04G-M627-X03U_KNT
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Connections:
- C1 pad 1: /PER0_P -> /PCIE_Slot/PCIE_TXp
- C1 pad 2: /PCIexpress_connector/_PER0_P -> Net-(U1C-PCIE_TXDP)
- C10 pad 1: /PCIexpress_connector/_PER4_N -> +3V3
- C10 pad 2: /PER4_N -> GND
- C11 pad 1: /PER5_P -> +3V3
- C11 pad 2: /PCIexpress_connector/_PER5_P -> GND
- C12 pad 1: /PCIexpress_connector/_PER5_N -> +3V3
- C12 pad 2: /PER5_N -> GND
- C13 pad 1: /PER6_P -> +3V3
- C13 pad 2: /PCIexpress_connector/_PER6_P -> GND
- C14 pad 1: /PCIexpress_connector/_PER6_N -> +3V3
- C14 pad 2: /PER6_N -> GND
- C15 pad 1: /PER7_P -> +3V3
- C15 pad 2: /PCIexpress_connector/_PER7_P -> GND
- C16 pad 1: /PCIexpress_connector/_PER7_N -> +3V3
- C16 pad 2: /PER7_N -> GND
- C2 pad 1: /PCIexpress_connector/_PER0_N -> /PCIE_Slot/PCIE_TXn
- C2 pad 2: /PER0_N -> Net-(U1C-PCIE_TXDN)
- C3 pad 1: /PER1_P -> +3V3
- C3 pad 2: /PCIexpress_connector/_PER1_P -> GND
- C4 pad 1: /PCIexpress_connector/_PER1_N -> +3V3
- C4 pad 2: /PER1_N -> GND
- C5 pad 1: /PER2_P -> Net-(U1A-+1.2VOUT_REG)
- C5 pad 2: /PCIexpress_connector/_PER2_P -> GND
- C6 pad 1: /PCIexpress_connector/_PER2_N -> +3V3
- C6 pad 2: /PER2_N -> GND
- C7 pad 1: /PER3_P -> +3V3
- C7 pad 2: /PCIexpress_connector/_PER3_P -> GND
- C8 pad 1: /PCIexpress_connector/_PER3_N -> +3V3
- C8 pad 2: /PER3_N -> GND
- C9 pad 1: /PER4_P -> +3V3
- C9 pad 2: /PCIexpress_connector/_PER4_P -> GND
- R1 pad 1: /PET0_N -> /PCIE_Slot/PCIE_WAKE
- R1 pad 2: GND -> +3V3
- R10 pad 1: /PET4_P -> +3V3
- R10 pad 2: GND -> Net-(U1D-USB3_OVCI_N)
- R11 pad 1: /PET5_N -> +3V3
- R11 pad 2: GND -> Net-(U1D-USB2_OVCI_N)
- R12 pad 1: /PET5_P -> +3V3
- R12 pad 2: GND -> Net-(U1D-USB1_OVCI_N)
- R13 pad 1: /PET6_N -> +3V3
- R13 pad 2: GND -> Net-(U1D-USB0_OVCI_N)
- R14 pad 1: /PET6_P -> Net-(U1D-USB0_IBREF)
- R15 pad 1: /PET7_N -> Net-(U1D-USB1_IBREF)
- R16 pad 1: /PET7_P -> Net-(U1D-USB2_IBERF)
- R2 pad 1: /PET0_P -> /PCIE_Slot/PeRST
- R2 pad 2: GND -> +3V3
- R3 pad 1: /PET1_N -> /PCIE_Slot/PCIE_CLKreq
- R3 pad 2: GND -> +3V3
- R4 pad 1: /PET1_P -> Net-(J1-~{WAKE})
- R4 pad 2: GND -> /PCIE_Slot/PCIE_WAKE
- R5 pad 1: /PET2_N -> Net-(J1-~{PERST})
- R5 pad 2: GND -> /PCIE_Slot/PeRST
- R6 pad 1: /PET2_P -> Net-(J1-~{PRSNT1})
- R6 pad 2: GND -> Net-(J1-~{PRSNT2}-PadB17)
- R7 pad 1: /PET3_N -> Net-(U1C-REXT)
- R8 pad 1: /PET3_P -> GND
- R8 pad 2: GND -> /PCIE_Slot/PCIE_CLKreq
- R9 pad 1: /PET4_N -> +3V3
- R9 pad 2: GND -> Net-(U1A-+1.2VOUT_REG)
- U10 pad 1: unconnected-(U10A-NC-Pad1) -> GND
- U10 pad 10: unconnected-(U10A-NC-Pad10) -> Net-(U10-XTAL_IN)
- U10 pad 11: unconnected-(U10A-NC-Pad11) -> Net-(U10-XTAL_OUT)
- U10 pad 12: unconnected-(U10A-VCC-Pad12) -> GND
- U10 pad 14: unconnected-(U10A-NC-Pad14) -> Net-(U10-VDD_FLASH_3.3_OUT)
- U10 pad 15: unconnected-(U10A-NC-Pad15) -> +3V3
- U10 pad 16: unconnected-(U10B-#CMD_LATCH_EN-Pad16) -> Net-(U10-V3.3_PHY_IN)
- U10 pad 17: unconnected-(U10B-ADDR_LATCH-Pad17) -> GND
- U10 pad 19: unconnected-(U10B-#WRITE_PROT-Pad19) -> Net-(U10-DATA2)
- U10 pad 2: unconnected-(U10A-NC-Pad2) -> GND
- U10 pad 20: unconnected-(U10A-NC-Pad20) -> Net-(U10-DATA3)
- U10 pad 21: unconnected-(U10A-NC-Pad21) -> Net-(U10-DATA4)
- U10 pad 22: unconnected-(U10A-NC-Pad22) -> Net-(U10-SDCMD)
- U10 pad 23: unconnected-(U10A-NC-Pad23) -> Net-(U10-DATA5)
- U10 pad 24: unconnected-(U10A-NC-Pad24) -> Net-(U10-SD_CLK)
- U10 pad 25: unconnected-(U10A-VSS-Pad25) -> Net-(U10-DATA6)
- U10 pad 26: unconnected-(U10A-NC-Pad26) -> Net-(U10-DATA7)
- U10 pad 27: unconnected-(U10A-NC-Pad27) -> Net-(U10-DATA0)
- U10 pad 28: unconnected-(U10A-NC-Pad28) -> Net-(U10-DATA1)
- U10 pad 3: unconnected-(U10A-NC-Pad3) -> Net-(U10-LED_ACTIVITY)
- U10 pad 4: unconnected-(U10A-NC-Pad4) -> Net-(U10-#CHIP_RST)
- U10 pad 5: unconnected-(U10A-NC-Pad5) -> Net-(U10-EXT_R)
- U10 pad 6: unconnected-(U10A-NC-Pad6) -> Net-(U10-V3.3_PHY_IN)
- U10 pad 7: unconnected-(U10B-STATUS-Pad7) -> USB3_DM
- U10 pad 8: unconnected-(U10B-#READ_EN-Pad8) -> USB3_DP
- U10 pad 9: unconnected-(U10B-#CHIP_EN-Pad9) -> GND
- U2 pad 1: unconnected-(U2-SDCDN-Pad1) -> Net-(U2-FB)
- U2 pad 2: unconnected-(U2-SDWP-Pad2) -> Net-(U2-EN)
- U2 pad 3: unconnected-(U2-LED_ACTIVITY-Pad3) -> Net-(U2-OCSET)
- U2 pad 4: unconnected-(U2-#CHIP_RST-Pad4) -> +12V
- U2 pad 5: unconnected-(U2-EXT_R-Pad5) -> Net-(D1-K)
- U2 pad 6: unconnected-(U2-V3.3_PHY_IN-Pad6) -> Net-(D1-K)
- U2 pad 7: unconnected-(U2-USB_DP-Pad7) -> GND
- U2 pad 8: unconnected-(U2-USB_DN-Pad8) -> GND
- U3 pad 1: unconnected-(U3A-NC-Pad1) -> Net-(U3-A0)
- U3 pad 2: unconnected-(U3A-NC-Pad2) -> Net-(U3-A1)
- U3 pad 3: unconnected-(U3A-NC-Pad3) -> Net-(U3-A2)
- U3 pad 4: unconnected-(U3A-NC-Pad4) -> GND
- U3 pad 5: unconnected-(U3A-NC-Pad5) -> Net-(U1E-EE_SDA)
- U3 pad 6: unconnected-(U3A-NC-Pad6) -> Net-(U1E-EE_SCL)
- U3 pad 7: unconnected-(U3B-STATUS-Pad7) -> Net-(U3-WP)
- U3 pad 8: unconnected-(U3B-#READ_EN-Pad8) -> +3V3
- U4 pad 1: unconnected-(U4-SDCDN-Pad1) -> GND
- U4 pad 10: unconnected-(U4-XTAL_IN-Pad10) -> Net-(U4-XTAL_IN)
- U4 pad 11: unconnected-(U4-XTAL_OUT-Pad11) -> Net-(U4-XTAL_OUT)
- U4 pad 12: unconnected-(U4-VSS-Pad12) -> GND
- U4 pad 14: unconnected-(U4-VDD_FLASH_3.3_OUT-Pad14) -> Net-(U4-VDD_FLASH_3.3_OUT)
- U4 pad 15: unconnected-(U4-AVDD_5.0-Pad15) -> +3V3
- U4 pad 16: unconnected-(U4-VDD__3.3_OUT-Pad16) -> Net-(U4-V3.3_PHY_IN)
- U4 pad 17: unconnected-(U4-VSSHM-Pad17) -> GND
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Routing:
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- added copper zone on B.Cu, net +12V
- added copper zone on F.Cu, net +12V
- added copper zone on F.Cu, net GND
- added copper zone on In1.Cu, net GND
- added copper zone on In2.Cu, net GND
- removed copper zone on B.Cu, net Net-(J2-+12V-PadA2)
- removed copper zone on F.Cu, net Net-(J2-+12V-PadA2)
- removed copper zone on B.Cu, net Net-(J2-GND-PadA12)
- removed copper zone on F.Cu, net Net-(J2-GND-PadA12)
- removed copper zone on In1.Cu, net Net-(J2-GND-PadA12)
- removed copper zone on In2.Cu, net Net-(J2-GND-PadA12)
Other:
- board size 456.8 x 111.2 mm -> 96.3 x 104.4 mm
- board text added: "J2"
- board text added: "Keep Out Cu"
- board text added: "Keep out components and traces both sides"
- board text added: "Keep out components and traces solder side"
- board text added: "Max component height: solder side 2,67mm component side 14,49mm"
